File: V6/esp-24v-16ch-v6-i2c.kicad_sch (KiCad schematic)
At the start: 24 parts, among them J9 SENSORS, SW2 1WIRE_SEL, U6 MCP23008-xSS, U7 MCP23008-xSS, U8 MCP23017x-x-SS, U9 DS2482S-100

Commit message: Revising power rails
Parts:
- renumbered C27 to C28, C28 to C29, C29 to C30, C30 to C31, C31 to C32, C32 to C33, C33 to C34, C34 to C35, C35 to C36, C36 to C37, C37 to C38

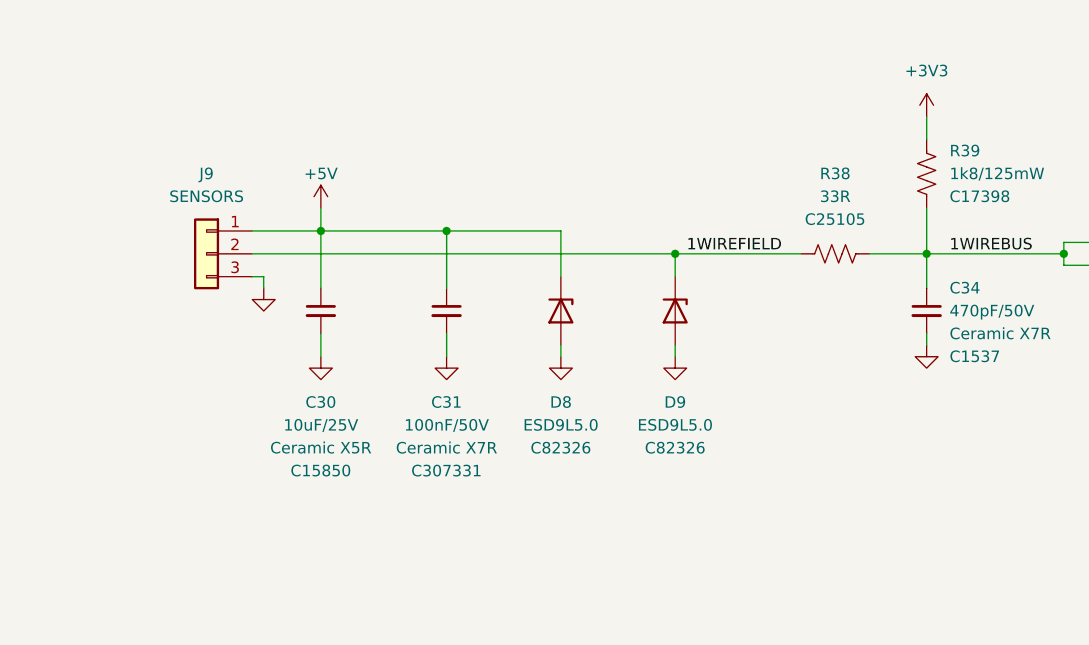
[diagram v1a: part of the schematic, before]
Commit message: ESP32 repositioned for shorter PHY traces.
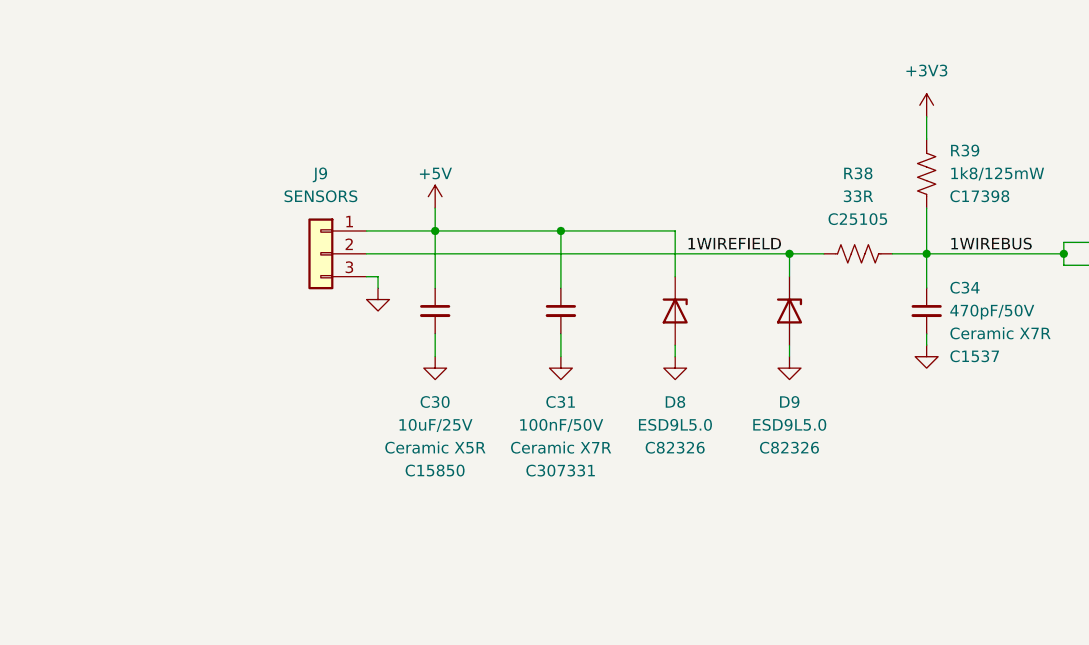
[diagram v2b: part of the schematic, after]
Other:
- moved on the sheet: C30, C31, D8, D9, J9, R38

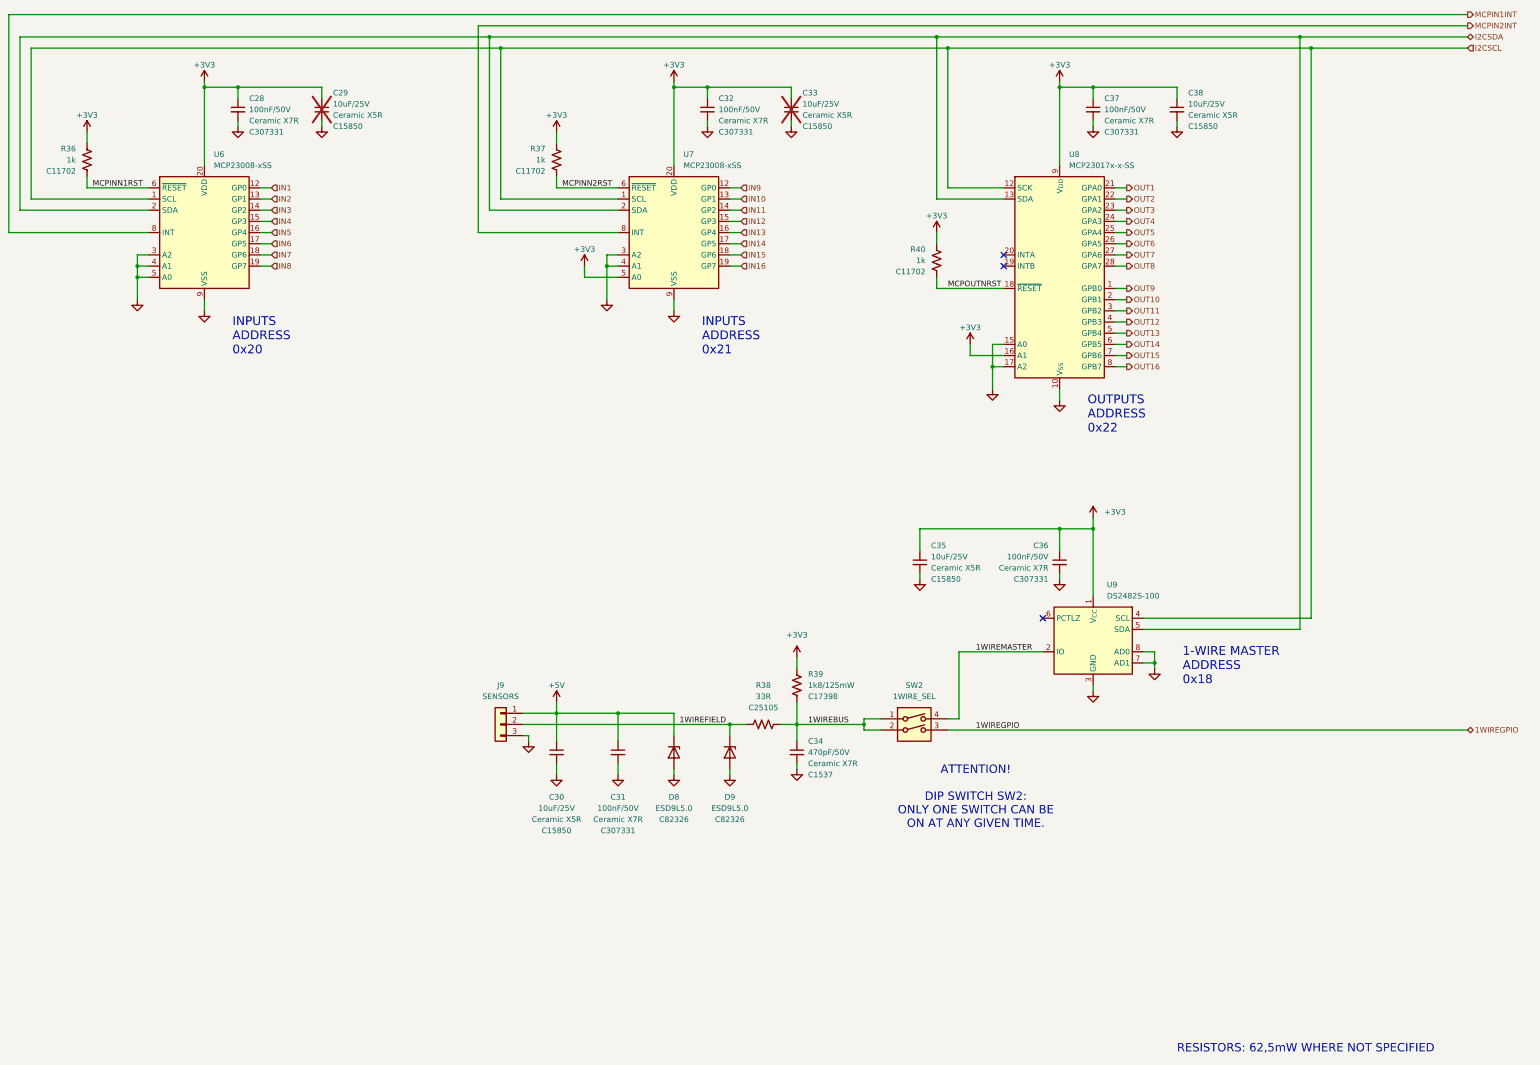
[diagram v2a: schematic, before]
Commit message: Included test points
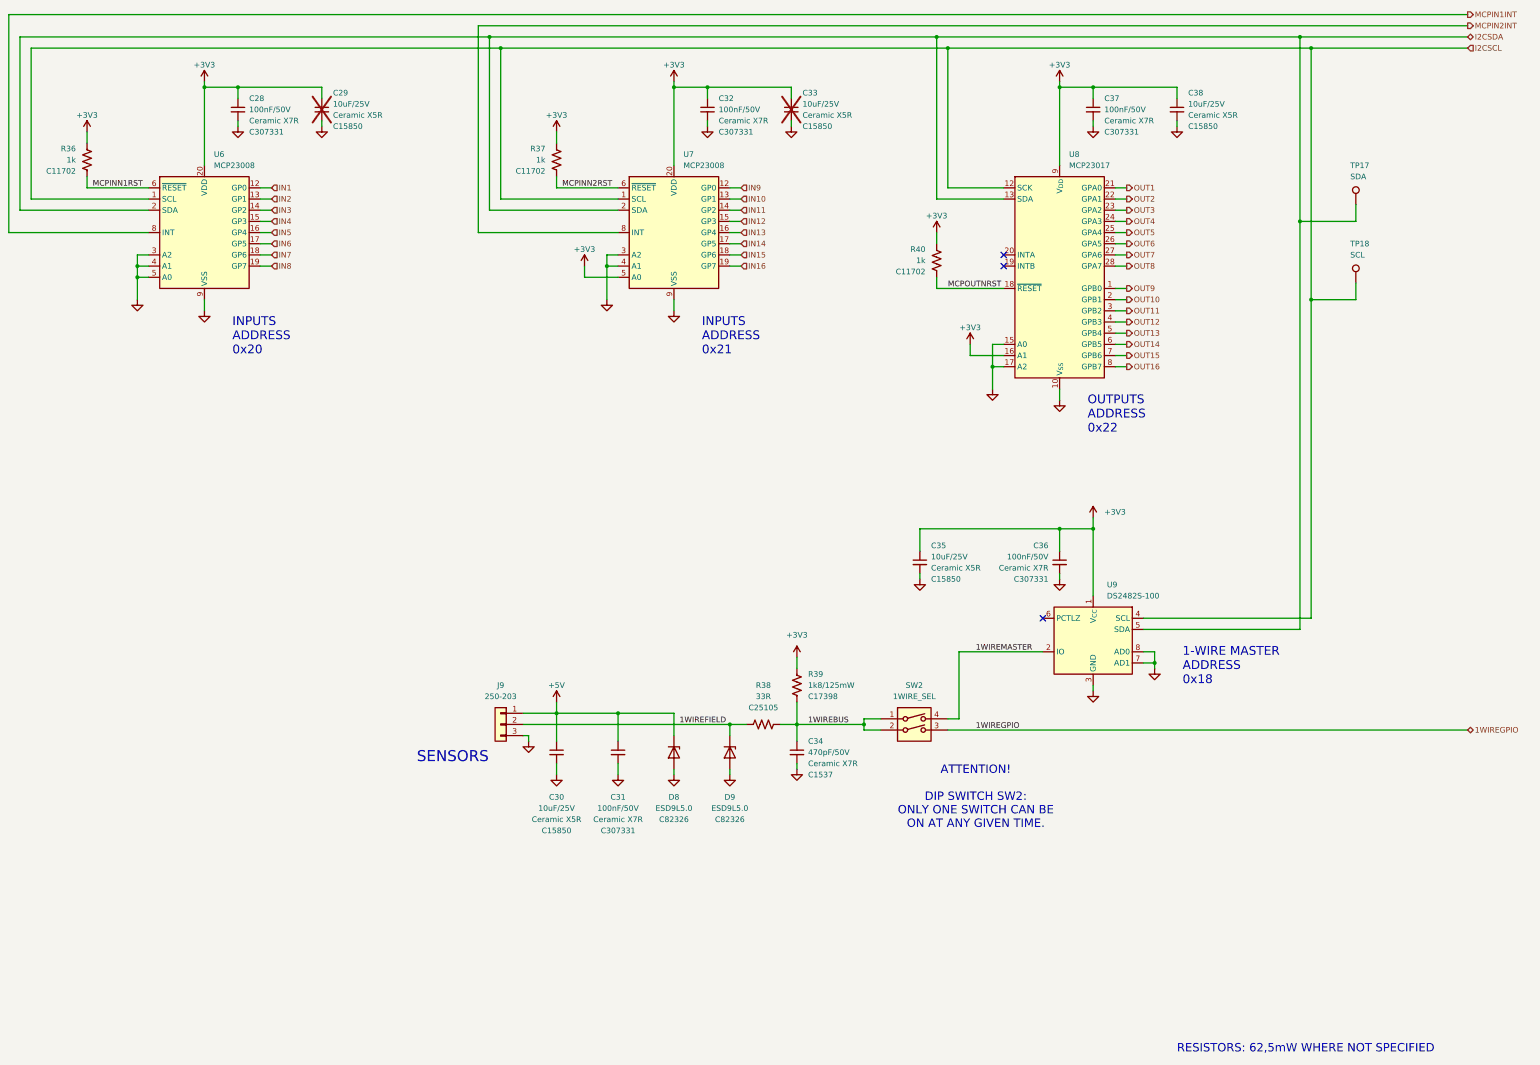
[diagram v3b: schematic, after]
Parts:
- added TP17: SDA, TestPoint:TestPoint_Pad_D1.5mm, symbol Connector:TestPoint
- added TP18: SCL, TestPoint:TestPoint_Pad_D1.5mm, symbol Connector:TestPoint
- J9: value SENSORS -> 250-203; LCSC Part # C2898745 -> C2765062; Mfr DIBO -> WAGO; Mfr PN DB141V-2.54-3P-GN -> 250-203; Vendor PN C2898745 -> C2765062
- U6, U7: value MCP23008-xSS -> MCP23008; Case (none) -> SSOP-20; JLCPCB BOM (none) -> 1; LCSC Part # (none) -> C148011; Mfr (none) -> Microchip; Mfr PN (none) -> MCP23008-E/SS; Vendor (none) -> JLCPCB; Vendor PN (none) -> C148011
- U8: value MCP23017x-x-SS -> MCP23017; Case (none) -> SSOP-28; JLCPCB BOM (none) -> 1; LCSC Part # (none) -> C506653; Mfr (none) -> Microchip; Mfr PN (none) -> MCP23017-E/SS; Vendor (none) -> JLCPCB; Vendor PN (none) -> C506653
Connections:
- net I2CSCL: now also TP18.1
- net I2CSDA: now also TP17.1
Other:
- note added: "SENSORS"

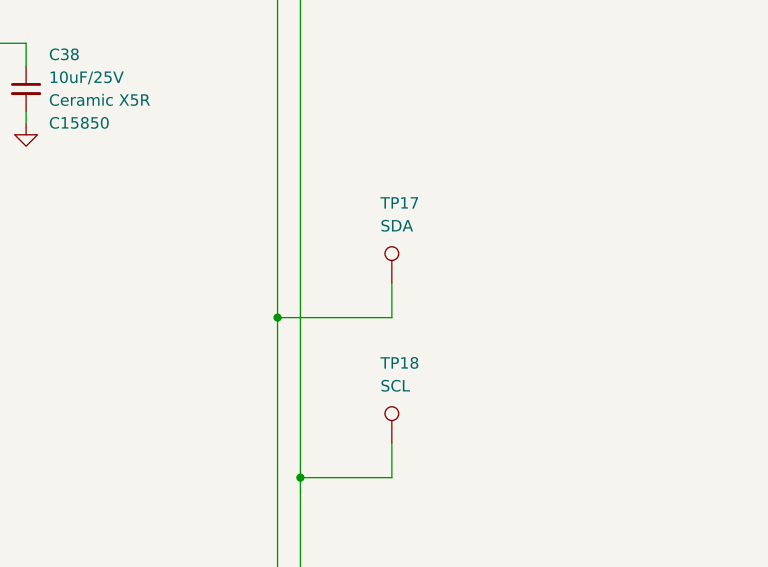
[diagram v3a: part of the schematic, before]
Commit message: Included a shunt resistor on the 5V rail, for measuring current during development.
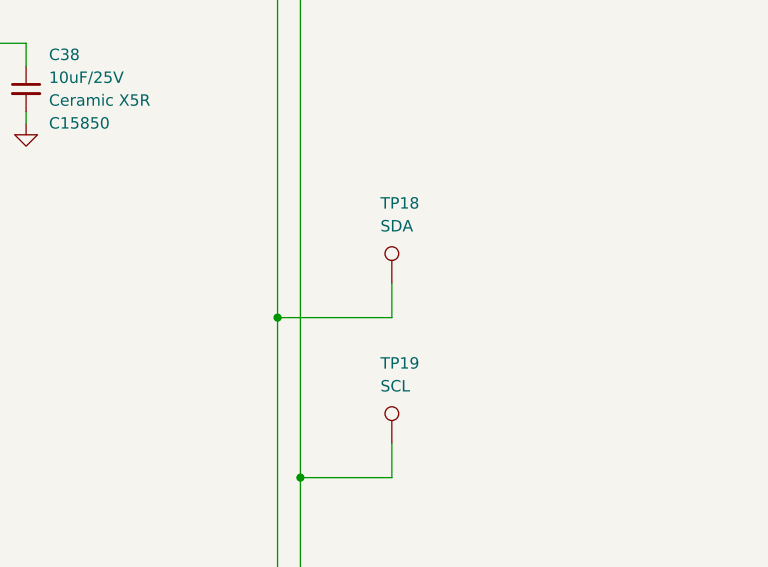
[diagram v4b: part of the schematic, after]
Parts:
- renumbered TP17 to TP18, TP18 to TP19
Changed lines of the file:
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@@
 		(in_pos_files yes)
 		(dnp no)
-		(property "Reference" "TP18"
+		(property "Reference" "TP19"
 			(at 344.17 76.2 0)
 			(show_name no)
@@
 			(project "esp-24v-16ch-v6"
 				(path "/2bc5a21a-1d79-419d-a592-6852cc07b00a/8d06b51d-d00b-4f80-9ffb-ab0131290cf2"
-					(reference "TP18")
+					(reference "TP19")
 					(unit 1)
 				)
@@
 		(in_pos_files yes)
 		(dnp no)
-		(property "Reference" "TP17"
+		(property "Reference" "TP18"
 			(at 344.17 58.42 0)
 			(show_name no)
@@
 			(project "esp-24v-16ch-v6"
 				(path "/2bc5a21a-1d79-419d-a592-6852cc07b00a/8d06b51d-d00b-4f80-9ffb-ab0131290cf2"
-					(reference "TP17")
+					(reference "TP18")
 					(unit 1)
 				)

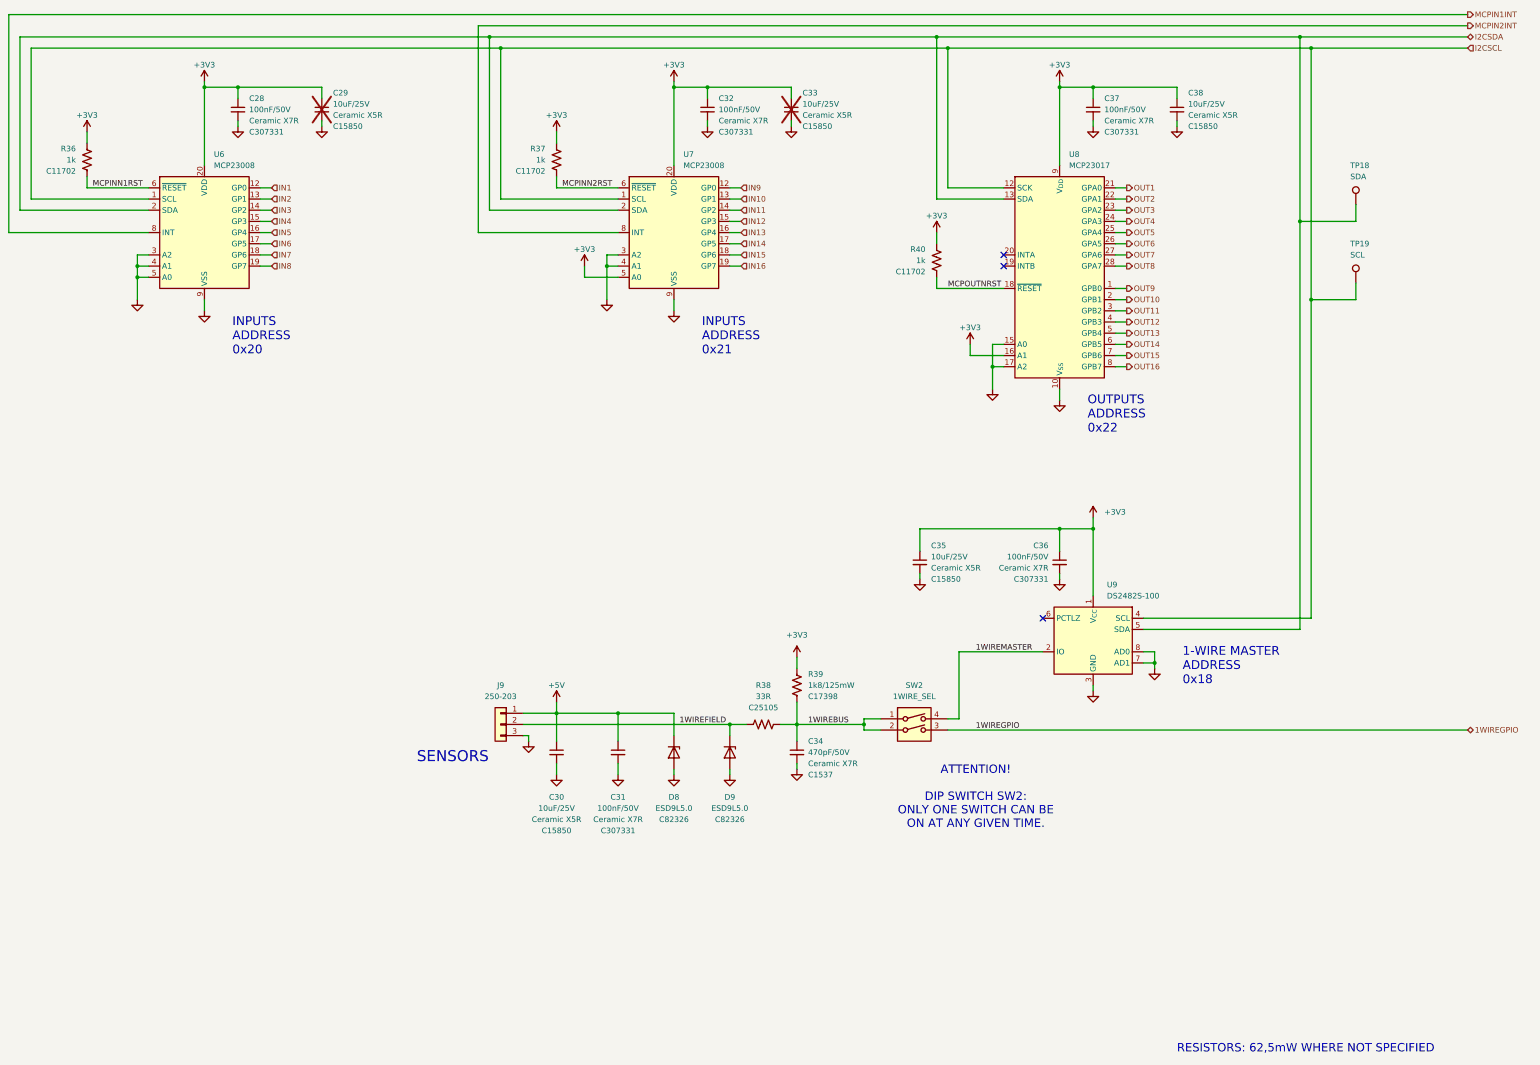
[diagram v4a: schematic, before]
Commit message: Added voltage monitors for both ESP32 and LAN8710A
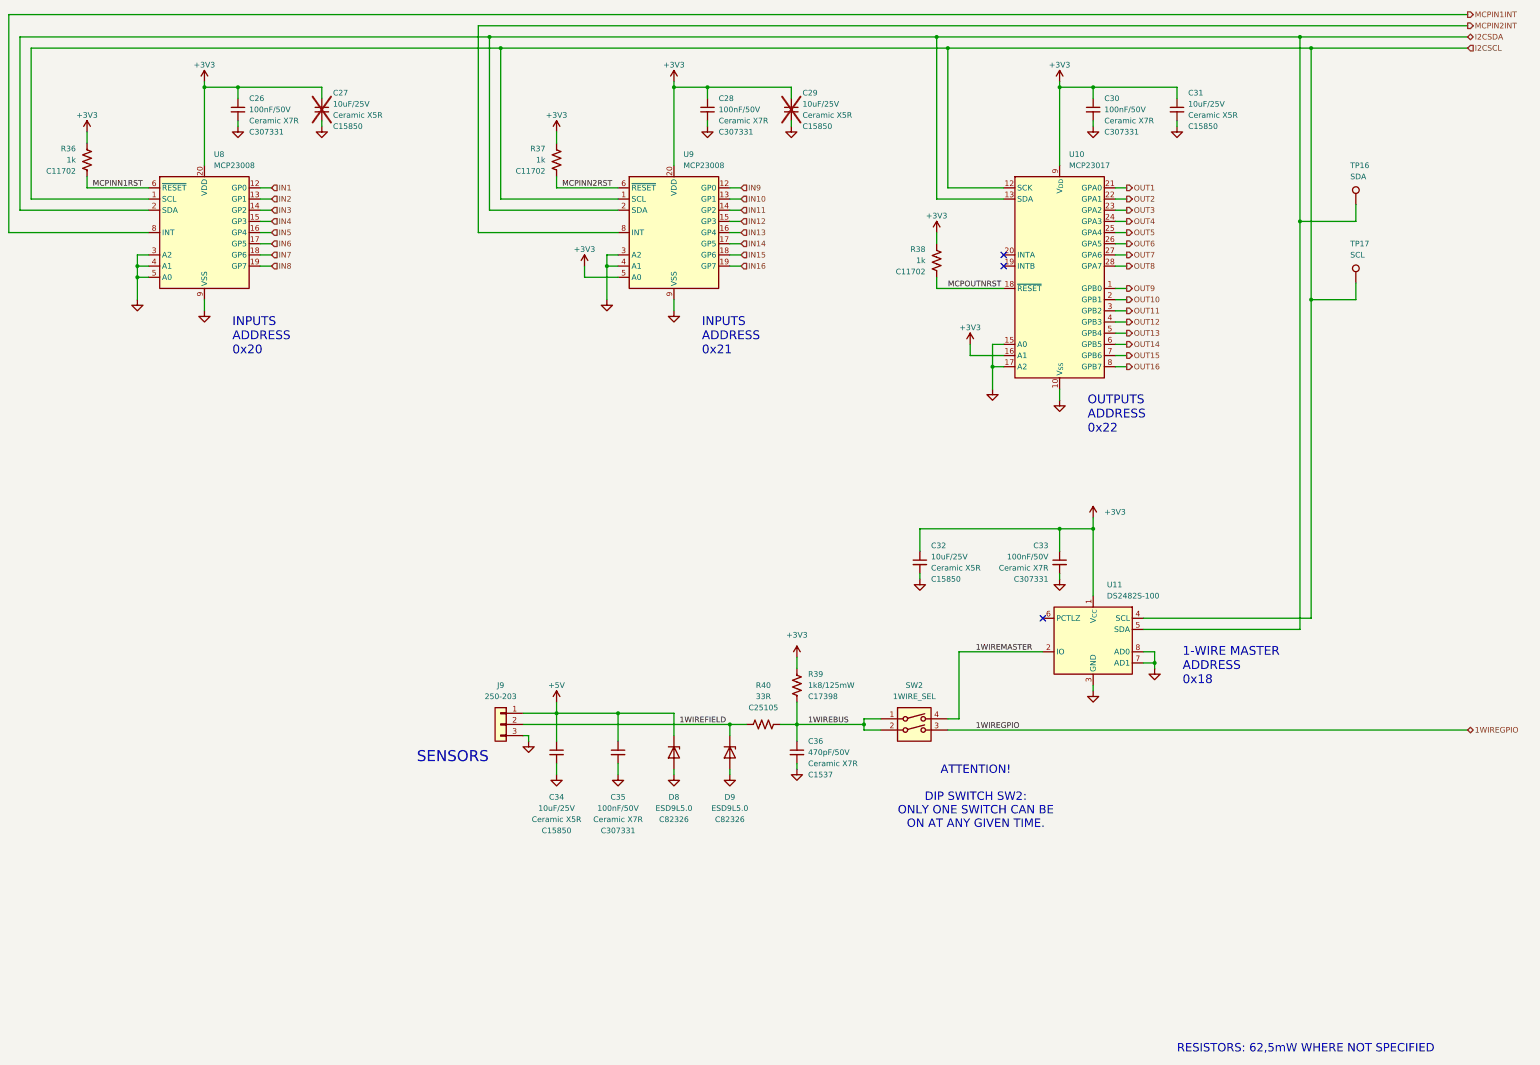
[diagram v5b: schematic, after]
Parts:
- renumbered C28 to C26, C29 to C27, C32 to C28, C33 to C29, C37 to C30, C38 to C31, C35 to C32, C36 to C33, C30 to C34, C31 to C35, C34 to C36, R40 to R38, R38 to R40, TP18 to TP16, TP19 to TP17, U8 to U10, U9 to U11, U6 to U8, U7 to U9
